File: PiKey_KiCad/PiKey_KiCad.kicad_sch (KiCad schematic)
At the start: 26 parts, among them SW1 BOOTSEL, SW2 RESET, U1 W25Q32JVSS, U2 RP2040, Y1 Crystal

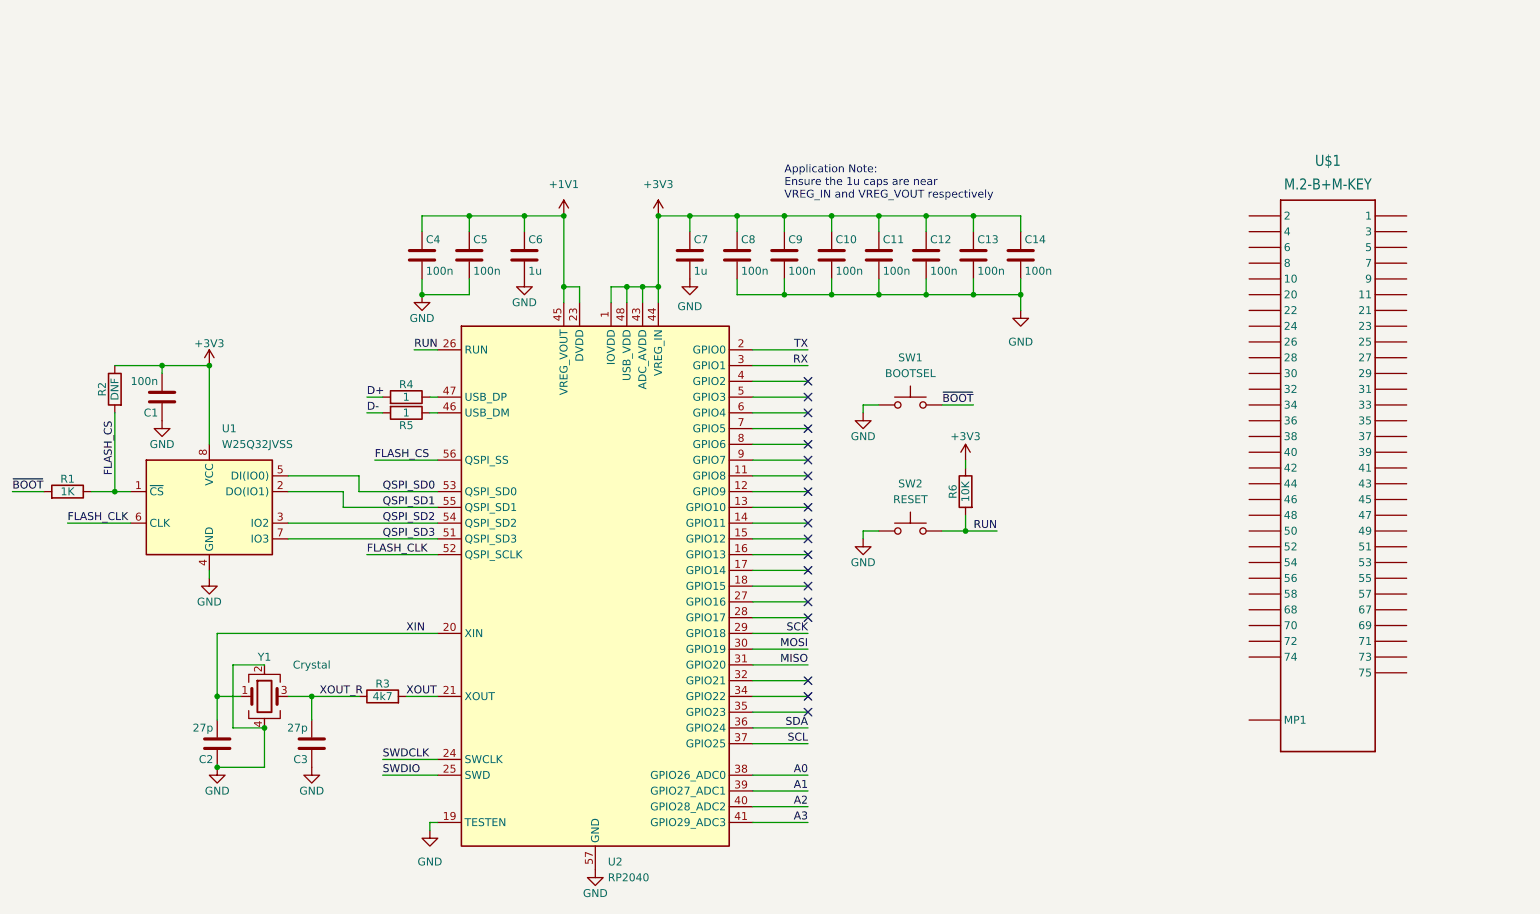
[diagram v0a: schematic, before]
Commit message: Initial routing
Need to finish routing power and connecting GNDs together.
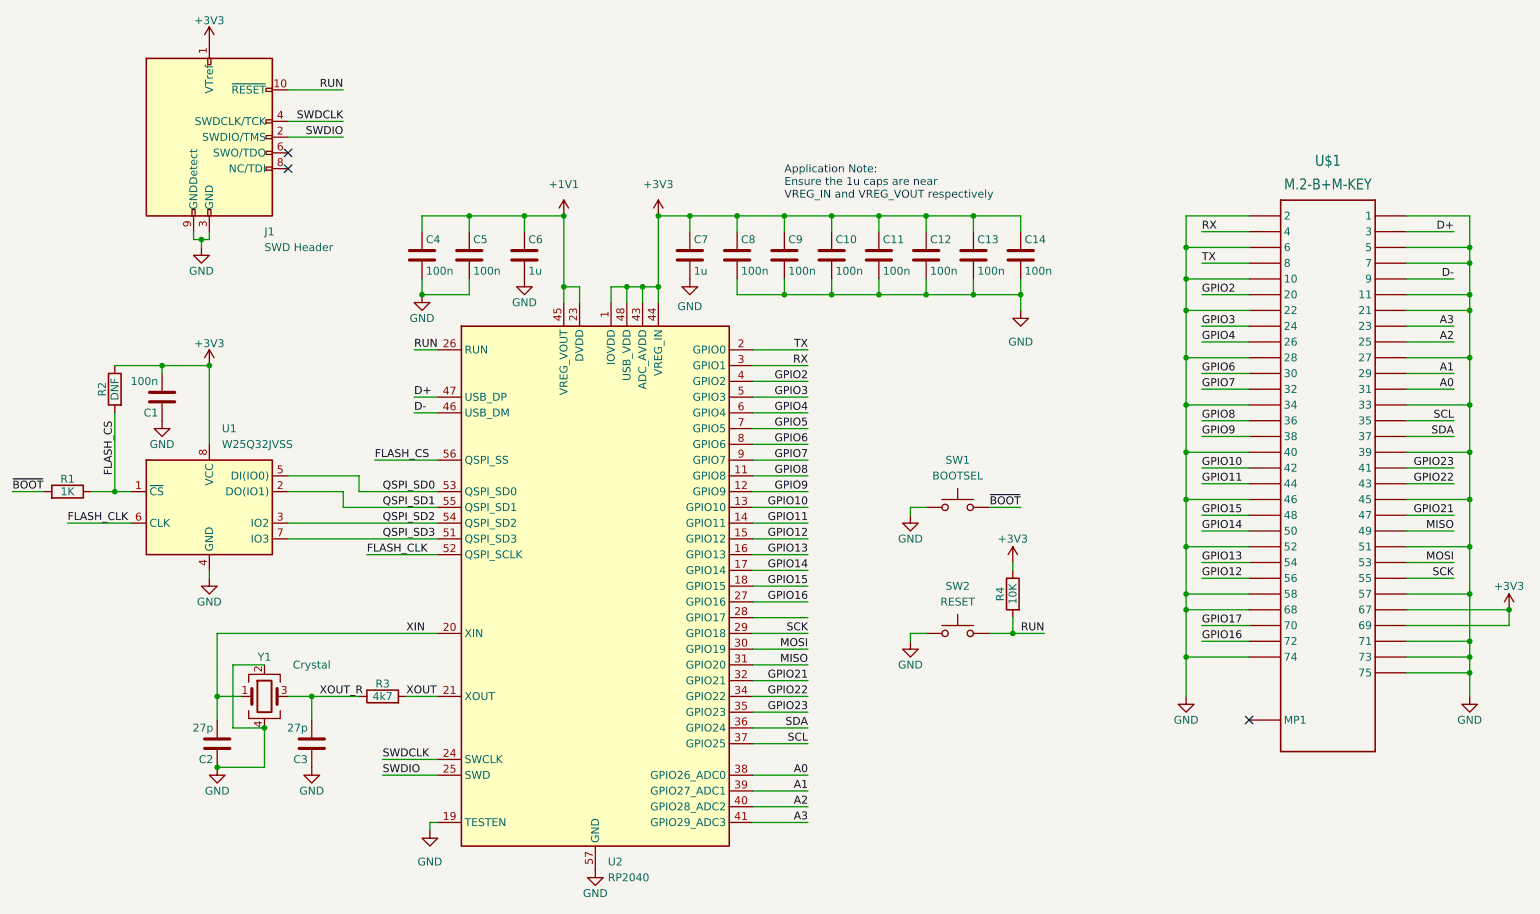
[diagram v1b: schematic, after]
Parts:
- removed R4, R5: 1, Resistor_SMD:R_0603_1608Metric_Pad0.98x0.95mm_HandSolder, symbol Device:R
- added J1: SWD Header, Connector_PinHeader_1.27mm:PinHeader_2x05_P1.27mm_Vertical_SMD, symbol Connector:Conn_ARM_JTAG_SWD_10
- C10, C11, C12, C13, C14, C4, C5, C6, C7, C8, C9: footprint Capacitor_SMD:C_0402_1005Metric_Pad0.74x0.62mm_HandSolder -> Capacitor_SMD:C_0402_1005Metric
- renumbered R6 to R4
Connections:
- net +3V3: now also U$1.P$67 (67), U$1.P$69 (69), J1.1 (VTref)
- net A0: now also U$1.P$31 (31)
- net A1: now also U$1.P$29 (29)
- net A2: now also U$1.P$25 (25)
- net A3: now also U$1.P$23 (23)
- net D+: now also U$1.P$3 (3), U2.47 (USB_DP)
- net D-: now also U$1.P$9 (9), U2.46 (USB_DM)
- net GND: now also U$1.P$1 (1), U$1.P$10 (10), U$1.P$11 (11), U$1.P$2 (2), U$1.P$21 (21), U$1.P$22 (22), U$1.P$27 (27), U$1.P$28 (28), U$1.P$33 (33), U$1.P$34 (34), U$1.P$39 (39), U$1.P$40 (40), U$1.P$45 (45), U$1.P$46 (46), U$1.P$5 (5), U$1.P$51 (51), U$1.P$52 (52), U$1.P$57 (57), U$1.P$58 (58), U$1.P$6 (6), U$1.P$68 (68), U$1.P$7 (7), U$1.P$71 (71), U$1.P$73 (73), U$1.P$74 (74), U$1.P$75 (75), J1.3 (GND), J1.5 (GND), J1.9 (GNDDetect)
- net MISO: now also U$1.P$49 (49)
- net MOSI: now also U$1.P$53 (53)
- net RUN: now also J1.10 (~{RESET})
- net RX: now also U$1.P$4 (4)
- net SCK: now also U$1.P$55 (55)
- net SCL: now also U$1.P$35 (35)
- net SDA: now also U$1.P$37 (37)
- net SWDCLK: now also J1.4 (SWDCLK/TCK)
- net SWDIO: now also J1.2 (SWDIO/TMS)
- net TX: now also U$1.P$8 (8)
- net GPIO2: now reaches U$1.P$20 (20)
- net GPIO2: now also U2.4 (GPIO2)
- net GPIO3: now reaches U$1.P$24 (24)
- net GPIO3: now also U2.5 (GPIO3)
- net GPIO4: now reaches U$1.P$26 (26)
- net GPIO4: now also U2.6 (GPIO4)
- net GPIO6: now reaches U$1.P$30 (30)
- net GPIO6: now also U2.8 (GPIO6)
- net GPIO7: now reaches U$1.P$32 (32)
- net GPIO7: now also U2.9 (GPIO7)
- net GPIO8: now reaches U$1.P$36 (36)
- net GPIO8: now also U2.11 (GPIO8)
- net GPIO9: now reaches U$1.P$38 (38)
- net GPIO9: now also U2.12 (GPIO9)
- net GPIO23: now reaches U$1.P$41 (41)
- net GPIO23: now also U2.35 (GPIO23)
- net GPIO10: now reaches U$1.P$42 (42)
- net GPIO10: now also U2.13 (GPIO10)
- net GPIO22: now reaches U$1.P$43 (43)
- net GPIO22: now also U2.34 (GPIO22)
- net GPIO11: now reaches U$1.P$44 (44)
- net GPIO11: now also U2.14 (GPIO11)
- net GPIO21: now reaches U$1.P$47 (47)
- net GPIO21: now also U2.32 (GPIO21)
- net GPIO15: now reaches U$1.P$48 (48)
- net GPIO15: now also U2.18 (GPIO15)
- net GPIO14: now reaches U$1.P$50 (50)
- net GPIO14: now also U2.17 (GPIO14)
- net GPIO13: now reaches U$1.P$54 (54)
- net GPIO13: now also U2.16 (GPIO13)
- net GPIO12: now reaches U$1.P$56 (56)
- net GPIO12: now also U2.15 (GPIO12)
- net GPIO17: now reaches U$1.P$70 (70)
- net GPIO16: now reaches U$1.P$72 (72)
- net GPIO16: now also U2.27 (GPIO16)
- net GPIO5: now reaches U2.7 (GPIO5)
- no-connect marks 19 -> 3
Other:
- moved on the sheet: R4, SW1, SW2

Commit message: Delay matching and stitching vias
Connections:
- net GPIO17 is gone; now on net GND: U$1.P$70 (70)
- net GND: now also U$1.P$72 (72), U$1.P$8 (8); no longer U$1.P$6 (6)
- net GPIO16: no longer U$1.P$72 (72)
- net TX: now also U$1.P$6 (6); no longer U$1.P$8 (8)

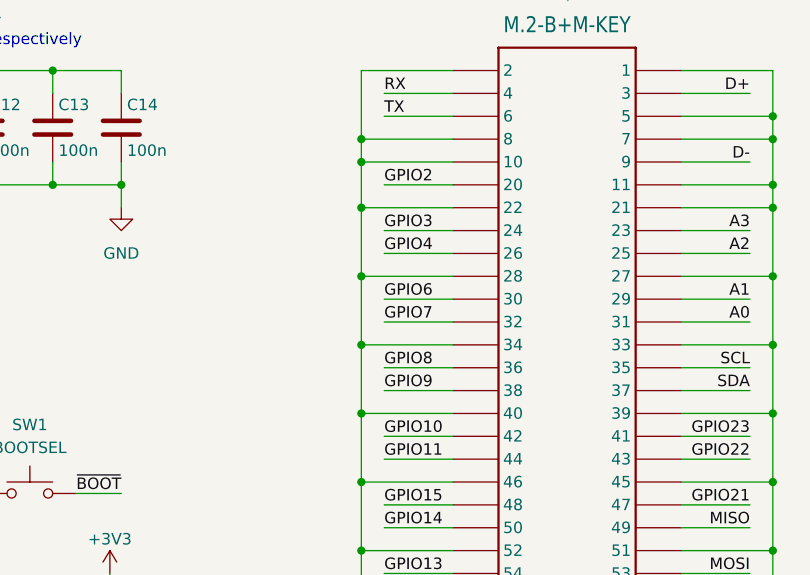
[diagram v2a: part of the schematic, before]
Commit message: Redid M.2 signals on back
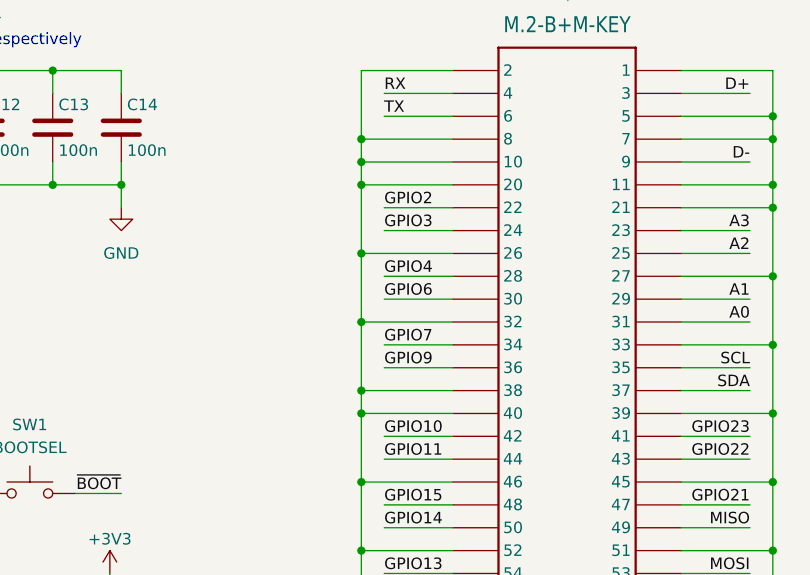
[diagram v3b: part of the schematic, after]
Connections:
- net GND: now also U$1.P$20 (20), U$1.P$26 (26), U$1.P$32 (32), U$1.P$38 (38); no longer U$1.P$22 (22), U$1.P$28 (28), U$1.P$34 (34)
- net GPIO2: now also U$1.P$22 (22); no longer U$1.P$20 (20)
- net GPIO4: now also U$1.P$28 (28); no longer U$1.P$26 (26)
- net GPIO7: now also U$1.P$34 (34); no longer U$1.P$32 (32)
- net GPIO8: no longer U$1.P$36 (36)
- net GPIO9: now also U$1.P$36 (36); no longer U$1.P$38 (38)
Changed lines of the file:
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@@
   (junction (at 62.23 128.27) (diameter 0) (color 0 0 0 0)
   )
-  (junction (at 218.44 73.66) (diameter 0) (color 0 0 0 0)
-  )
   (junction (at 264.16 66.04) (diameter 0) (color 0 0 0 0)
   )
@@
   (junction (at 184.15 50.8) (diameter 0) (color 0 0 0 0)
   )
+  (junction (at 218.44 78.74) (diameter 0) (color 0 0 0 0)
+  )
   (junction (at 69.85 133.35) (diameter 0) (color 0 0 0 0)
   )
@@
   (junction (at 218.44 60.96) (diameter 0) (color 0 0 0 0)
   )
+  (junction (at 218.44 63.5) (diameter 0) (color 0 0 0 0)
+  )
   (junction (at 138.43 50.8) (diameter 0) (color 0 0 0 0)
   )
@@
   (junction (at 60.96 74.93) (diameter 0) (color 0 0 0 0)
   )
-  (junction (at 218.44 66.04) (diameter 0) (color 0 0 0 0)
-  )
   (junction (at 191.77 63.5) (diameter 0) (color 0 0 0 0)
   )
@@
   (junction (at 102.87 50.8) (diameter 0) (color 0 0 0 0)
   )
+  (junction (at 218.44 86.36) (diameter 0) (color 0 0 0 0)
+  )
   (junction (at 45.72 95.25) (diameter 0) (color 0 0 0 0)
   )
@@
   (junction (at 176.53 63.5) (diameter 0) (color 0 0 0 0)
   )
+  (junction (at 218.44 71.12) (diameter 0) (color 0 0 0 0)
+  )
   (junction (at 133.35 50.8) (diameter 0) (color 0 0 0 0)
   )
@@
   )
   (junction (at 264.16 88.9) (diameter 0) (color 0 0 0 0)
-  )
-  (junction (at 218.44 81.28) (diameter 0) (color 0 0 0 0)
   )
   (no_connect (at 228.6 132.08))
@@
     (stroke (width 0) (type default))
   )
+  (wire (pts (xy 220.98 73.66) (xy 228.6 73.66))
+    (stroke (width 0) (type default))
+  )
   (wire (pts (xy 95.25 60.96) (xy 95.25 63.5))
     (stroke (width 0) (type default))
@@
     (stroke (width 0) (type default))
   )
+  (wire (pts (xy 218.44 86.36) (xy 218.44 88.9))
+    (stroke (width 0) (type default))
+  )
   (wire (pts (xy 173.99 119.38) (xy 173.99 118.11))
     (stroke (width 0) (type default))
@@
     (stroke (width 0) (type default))
   )
-  (wire (pts (xy 218.44 60.96) (xy 218.44 66.04))
+  (wire (pts (xy 218.44 60.96) (xy 218.44 63.5))
     (stroke (width 0) (type default))
   )
@@
     (stroke (width 0) (type default))
   )
-  (wire (pts (xy 228.6 66.04) (xy 218.44 66.04))
-    (stroke (width 0) (type default))
-  )
   (wire (pts (xy 148.59 135.89) (xy 157.48 135.89))
     (stroke (width 0) (type default))
@@
     (stroke (width 0) (type default))
   )
+  (wire (pts (xy 218.44 78.74) (xy 228.6 78.74))
+    (stroke (width 0) (type default))
+  )
   (wire (pts (xy 93.98 80.01) (xy 97.79 80.01))
     (stroke (width 0) (type default))
@@
     (stroke (width 0) (type default))
   )
+  (wire (pts (xy 218.44 63.5) (xy 218.44 71.12))
+    (stroke (width 0) (type default))
+  )
   (wire (pts (xy 218.44 111.76) (xy 218.44 104.14))
     (stroke (width 0) (type default))
@@
     (stroke (width 0) (type default))
   )
-  (wire (pts (xy 228.6 81.28) (xy 218.44 81.28))
-    (stroke (width 0) (type default))
-  )
   (wire (pts (xy 218.44 114.3) (xy 228.6 114.3))
     (stroke (width 0) (type default))
@@
     (stroke (width 0) (type default))
   )
-  (wire (pts (xy 228.6 73.66) (xy 218.44 73.66))
-    (stroke (width 0) (type default))
-  )
   (wire (pts (xy 218.44 114.3) (xy 218.44 116.84))
     (stroke (width 0) (type default))
@@
     (stroke (width 0) (type default))
   )
+  (wire (pts (xy 218.44 78.74) (xy 218.44 86.36))
+    (stroke (width 0) (type default))
+  )
   (wire (pts (xy 254 68.58) (xy 261.62 68.58))
     (stroke (width 0) (type default))
@@
     (stroke (width 0) (type default))
   )
-  (wire (pts (xy 228.6 71.12) (xy 220.98 71.12))
+  (wire (pts (xy 218.44 71.12) (xy 228.6 71.12))
     (stroke (width 0) (type default))
   )
@@
     (stroke (width 0) (type default))
   )
+  (wire (pts (xy 220.98 81.28) (xy 228.6 81.28))
+    (stroke (width 0) (type default))
+  )
   (wire (pts (xy 118.11 64.77) (xy 118.11 62.23))
     (stroke (width 0) (type default))
@@
     (stroke (width 0) (type default))
   )
-  (wire (pts (xy 218.44 73.66) (xy 218.44 66.04))
-    (stroke (width 0) (type default))
-  )
   (wire (pts (xy 176.53 60.96) (xy 176.53 63.5))
     (stroke (width 0) (type default))
@@
     (stroke (width 0) (type default))
   )
-  (wire (pts (xy 218.44 81.28) (xy 218.44 73.66))
+  (wire (pts (xy 218.44 71.12) (xy 218.44 78.74))
     (stroke (width 0) (type default))
   )
@@
     (stroke (width 0) (type default))
   )
-  (wire (pts (xy 218.44 88.9) (xy 218.44 81.28))
+  (wire (pts (xy 220.98 66.04) (xy 228.6 66.04))
     (stroke (width 0) (type default))
   )
@@
     (stroke (width 0) (type default))
   )
-  (wire (pts (xy 220.98 63.5) (xy 228.6 63.5))
+  (wire (pts (xy 218.44 63.5) (xy 228.6 63.5))
     (stroke (width 0) (type default))
   )
@@
     (stroke (width 0) (type default))
   )
-  (wire (pts (xy 228.6 86.36) (xy 220.98 86.36))
+  (wire (pts (xy 218.44 86.36) (xy 228.6 86.36))
     (stroke (width 0) (type default))
   )
@@
   )
   (wire (pts (xy 102.87 60.96) (xy 102.87 63.5))
-    (stroke (width 0) (type default))
-  )
-  (wire (pts (xy 228.6 78.74) (xy 220.98 78.74))
     (stroke (width 0) (type default))
   )
@@
     (effects (font (size 1.27 1.27)) (justify left bottom))
   )
-  (label "GPIO9" (at 220.98 86.36 0) (fields_autoplaced)
+  (label "GPIO9" (at 220.98 83.82 0) (fields_autoplaced)
     (effects (font (size 1.27 1.27)) (justify left bottom))
   )
@@
     (effects (font (size 1.27 1.27)) (justify right bottom))
   )
-  (label "GPIO4" (at 220.98 71.12 0) (fields_autoplaced)
+  (label "GPIO4" (at 220.98 73.66 0) (fields_autoplaced)
     (effects (font (size 1.27 1.27)) (justify left bottom))
   )
@@
     (effects (font (size 1.27 1.27)) (justify right bottom))
   )
+  (label "GPIO2" (at 220.98 66.04 0) (fields_autoplaced)
+    (effects (font (size 1.27 1.27)) (justify left bottom))
+  )
   (label "RUN" (at 82.55 30.48 180) (fields_autoplaced)
     (effects (font (size 1.27 1.27)) (justify right bottom))
@@
     (effects (font (size 1.27 1.27)) (justify left bottom))
   )
-  (label "GPIO7" (at 220.98 78.74 0) (fields_autoplaced)
+  (label "GPIO7" (at 220.98 81.28 0) (fields_autoplaced)
     (effects (font (size 1.27 1.27)) (justify left bottom))
   )
@@
     (effects (font (size 1.27 1.27)) (justify right bottom))
   )
-  (label "GPIO8" (at 220.98 83.82 0) (fields_autoplaced)
-    (effects (font (size 1.27 1.27)) (justify left bottom))
-  )
   (label "RUN" (at 93.98 72.39 0) (fields_autoplaced)
     (effects (font (size 1.27 1.27)) (justify left bottom))
@@
     (effects (font (size 1.27 1.27)) (justify right bottom))
   )
-  (label "GPIO2" (at 220.98 63.5 0) (fields_autoplaced)
-    (effects (font (size 1.27 1.27)) (justify left bottom))
-  )
   (label "GPIO4" (at 157.48 82.55 180) (fields_autoplaced)

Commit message: Fixed page settings, added BOM
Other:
- title: (none) -> PiKey: RP2040 M.2 B+M SoM
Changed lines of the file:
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@@
 (kicad_sch (version 20230121) (generator eeschema)
   (paper "A4")
+  (title_block
+    (title "PiKey: RP2040 M.2 B+M SoM")
+    (date "2023-09-15")
+    (rev "v1.0")
+  )
   (junction (at 146.05 50.8) (diameter 0) (color 0 0 0 0)
   )
